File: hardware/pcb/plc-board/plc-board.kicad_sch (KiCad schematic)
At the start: 29 parts, among them J1 MAINS_L_N, J2 ESP32_UART0_PROGRAMMING, J3 ST7580_JTAG_DEBUG, U1 HLK-5M05, U2 ESP32-C3-MINI-1, U3 AMS1117-3.3, U4 ST7580, Y1 8MHz

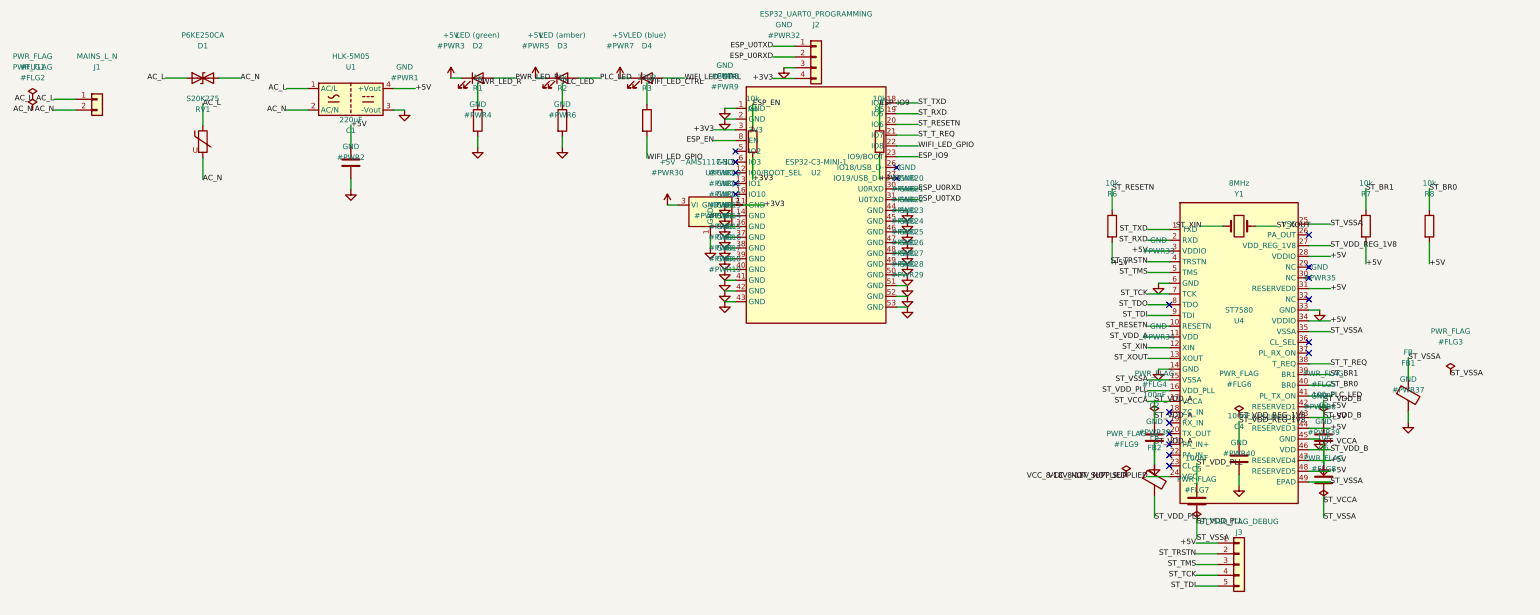
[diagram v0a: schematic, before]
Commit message: hardware: power the PLC Adapter from the Terminal, remove the inverter
Board 1's remaining gaps were meant to be a power-electronics design task:
supply the ST7580's 8-18V VCC, drive the IRF540N inverter, define its
topology. Two findings made those questions the wrong ones.

The adapter had no power source during an outage. Its only supply is the
HLK-5M05, which needs 90-264V AC. When the grid fails the adapter stops --
so it could never have run an inverter, and the 24V it was supposed to
inject could not have powered a neighbouring adapter either, despite
docs/inverter-master.md stating that a slave "listens on the wire powered
by the master's 24V injection". hardware/bom.md gives Board 1 no battery
and no supercapacitor; every battery line in that file belongs to the
Terminal. The firmware protocol had already been written against a battery
that never existed: MASTER_ALIVE carries battery_pct, MASTER_RESIGN
defines reason 0x01 = low battery.

The 24V injection was also outside EN 50065-1. The A-band limit is
134 dB(uV) at 9 kHz falling to 120 dB(uV) at 95 kHz -- 5 Vrms down to
1 Vrms -- so 24V is 5-24x over. docs/electrical-safety.md claimed the
injection was "within these limits"; it was not. The same section listed
GRIDNET among the A-band's permitted users alongside energy companies, but
the A-band is allocated to electricity suppliers and general equipment
belongs in 95-148.5 kHz. Separately, the ST7580's own PA delivers 14 V p-p
= 4.95 Vrms: ST sized the part to land on that limit, so the chip already
produces the strongest signal the standard permits.

So the adapter is now powered from the Terminal's battery over a
detachable USB-C cable, and the inverter is gone -- what it was for is
done either by that cable or by a properly-supplied power amplifier.

Board 1 schematic (29 -> 47 components, ERC clean, 0 errors):

- USB-C sink inlet (J4) with 5.1k CC strapping, power-only. It sits on the
  HLK-5M05's isolated secondary, which now matters more than before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
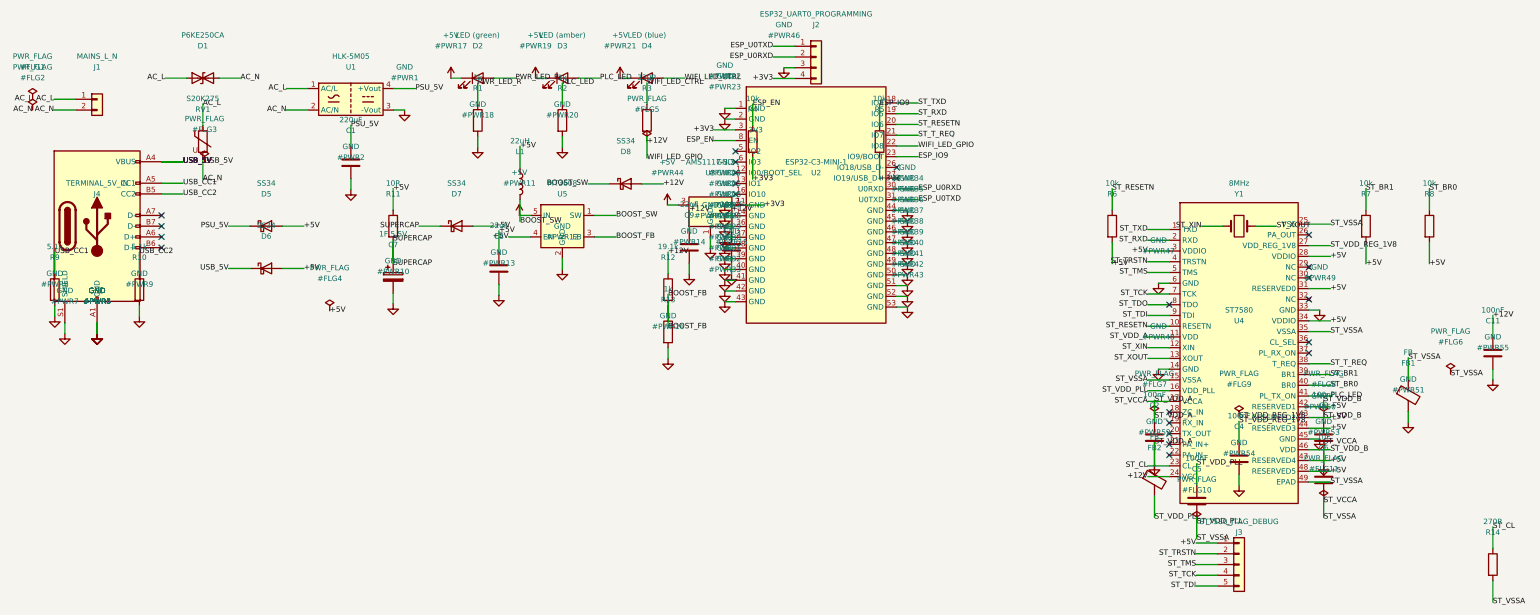
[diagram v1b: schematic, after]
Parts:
- added C10: 100uF, Capacitor_THT:CP_Radial_D6.3mm_P2.50mm, symbol Device:C
- added C11: 100nF, Capacitor_SMD:C_0603_1608Metric, symbol Device:C
- added C7: 1F 5.5V, Capacitor_THT:CP_Radial_D10.0mm_P5.00mm, symbol Device:C_Polarized
- added C8, C9: 22uF, Capacitor_SMD:C_1206_3216Metric, symbol Device:C
- added D5, D6, D7, D8: SS34, Diode_SMD:D_SMA, symbol Device:D_Schottky
- added J4: TERMINAL_5V_IN, Connector_USB:USB_C_Receptacle_HRO_TYPE-C-31-M-12, symbol Connector:USB_C_Receptacle_USB2.0_14P
- added L1: 22uH, Inductor_SMD:L_6.3x6.3_H3, symbol Device:L
- added R10, R9: 5.1k, Resistor_SMD:R_0603_1608Metric, symbol Device:R
- added R11: 10R, Resistor_SMD:R_1206_3216Metric, symbol Device:R
- added R12: 19.1k, Resistor_SMD:R_0603_1608Metric, symbol Device:R
- added R13: 1k, Resistor_SMD:R_0603_1608Metric, symbol Device:R
- added R14: 270R, Resistor_SMD:R_0603_1608Metric, symbol Device:R
- added U5: MT3608, Package_TO_SOT_SMD:SOT-23-6, symbol Regulator_Switching:MT3608
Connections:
- net WIFI_LED_GPIO is gone; now on net +12V: R3.2, U2.22 (IO8)
- net +5V: now also C8.1, D5.2 (A), D6.2 (A), D7.2 (A), L1.1, R11.1, U5.4 (EN), U5.5 (IN); no longer C1.1, U1.4 (+Vout)
- net GND: now also C10.2, C11.2, C7.2, C8.2, C9.2, J4.A1 (GND), J4.A12 (GND), J4.B1 (GND), J4.B12 (GND), J4.S1 (SHIELD), R10.2, R13.2, R14.2, R9.2, U5.2 (GND)
- net ST_CL: now reaches U4.23 (CL)
- net ST_CL: now also R14.1
- net VCC_8-18V_NOT_SUPPLIED renamed +12V
- net +12V: now also C10.1, C11.1, C9.1, D8.2 (A), R12.1
- new net BOOST_FB: R12.2, R13.1, U5.3 (FB)
- new net BOOST_SW: D8.1 (K), L1.2, U5.1 (SW)
- new net PSU_5V: C1.1, D5.1 (K), U1.4 (+Vout)
- new net SUPERCAP: C7.1, D7.1 (K), R11.2
- new net USB_5V: D6.1 (K), J4.A4 (VBUS), J4.A9 (VBUS), J4.B4 (VBUS), J4.B9 (VBUS)
- new net USB_CC1: J4.A5 (CC1), R9.1
- new net USB_CC2: J4.B5 (CC2), R10.1
- no-connect marks 20 -> 23

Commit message: hardware: build Board 1's line coupling, retuned from AN4068 to B+C
The last open block on Board 1, and the reason its PCB layout had not
started. The ST7580 datasheet specifies the PA's pins but not the network
hung off them; AN4068 does, and earlier passes could not retrieve it.

It was read through alldatasheet's HTML viewer, which carries each page's
text even though the page images come back blank. That gives the values,
the equations and the tables -- but not Figure 6 (the coupling schematic)
or Figure 14 (the zero crossing circuit), which are images with no text
layer. Where connectivity could not be read off a figure it is derived from
the equations, and docs/plc-coupling.md says so at each point.

The values are not AN4068's. Its reference design is a CENELEC A-band node:
receive filter on 80 kHz, coupling resonance on 85 kHz, receive sensitivity
specified at fC = 86 kHz. A-band is allocated to electricity suppliers
(docs/electrical-safety.md), so GRIDNET sits in B+C, 95-140 kHz -- which
puts our entire band on the skirt of their filters. Three rules, applied to
every block:

- keep AN4068's Q values, which it chose against measured mains impedance
  and a Montecarlo tolerance analysis this project cannot repeat;
- keep its ratios to the band edge rather than its absolute corners;
- move reactances, not resistors.

                        AN4068 (A-band)        this board (B+C)
  TX RC pre-filter      1.5k + 1nF, 106 kHz    1k + 1nF, 159 kHz
  TX Sallen-Key         150 kHz, Q 1.03        221 kHz, Q 1.03  (100pF -> 68pF)
  PA gain               4.3 = 12.7 dB          4.3 = 12.7 dB    (unchanged)
  RX resonance          220uH/18nF, 80 kHz     150uH/12nF, 118.6 kHz
  Line coupling         15uH/220nF, 85 kHz     12uH/150nF, 114 kHz

Every resistor keeps its reference value. That is not a stylistic choice --
it falls out of solving for the new centres with E-series parts, and it
leaves the gain and Q expressions (resistor ratios) untouched.

Each block was check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
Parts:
- added C12: 1nF C0G, Capacitor_SMD:C_0603_1608Metric, symbol Device:C
- added C13, C14: 68pF C0G, Capacitor_SMD:C_0603_1608Metric, symbol Device:C
- added C15: 12nF, Capacitor_SMD:C_0603_1608Metric, symbol Device:C
- added C16: 10uF/50V X5R, Capacitor_SMD:C_1210_3225Metric, symbol Device:C
- added C17: 150nF X1, Capacitor_THT:C_Rect_L16.5mm_W5.0mm_P15.00mm_MKT, symbol Device:C
- added L2: 150uH, Inductor_SMD:L_1210_3225Metric, symbol Device:L
- added L3: 12uH, Inductor_SMD:L_7.3x7.3_H4.5, symbol Device:L
- added R15: 1k, Resistor_SMD:R_0603_1608Metric, symbol Device:R
- added R16: 5.1k, Resistor_SMD:R_0603_1608Metric, symbol Device:R
- added R17: 22k, Resistor_SMD:R_0603_1608Metric, symbol Device:R
- added R18: 33k, Resistor_SMD:R_0603_1608Metric, symbol Device:R
- added R19: 10k, Resistor_SMD:R_0603_1608Metric, symbol Device:R
- added R20: 150R, Resistor_SMD:R_0603_1608Metric, symbol Device:R
- added T1: 750510231, gridnet_footprints:Transformer_Wuerth_750510231, symbol gridnet_parts:PLC_COUPLING_TRANSFORMER
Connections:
- net AC_L: now also C17.2
- net AC_N: now also T1.7 (SEC_B)
- net GND: now also C12.2, C14.2, C15.2, L2.2, R19.2, T1.4 (PRI_B)
- net ST_RX_IN: now reaches U4.19 (RX_IN)
- net ST_RX_IN: now also C15.1, L2.1, R20.2
- net ST_TX_OUT: now reaches U4.20 (TX_OUT)
- net ST_TX_OUT: now also R15.1
- net ST_PA_IN_P: now reaches U4.21 (PA_IN+)
- net ST_PA_IN_P: now also C14.1, R17.2
- net ST_PA_IN_N: now reaches U4.22 (PA_IN-)
- net ST_PA_IN_N: now also R18.2, R19.1
- net ST_PA_OUT: now reaches U4.26 (PA_OUT)
- net ST_PA_OUT: now also C13.2, C16.1, R18.1
- new net PLC_COUPLING: C16.2, R20.1, T1.1 (PRI_A)
- new net PLC_LINE: L3.1, T1.10 (SEC_A)
- new net PLC_LINE_X1: C17.1, L3.2
- new net ST_PA_SK: C13.1, R16.2, R17.1
- new net ST_TX_FILT: C12.1, R15.2, R16.1
- no-connect marks 23 -> 18

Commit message: hardware: place Board 1's PCB around a mains isolation barrier
plc-board.kicad_pcb places all 62 components inside the 100x80mm outline,
with thermal vias under both exposed pads and the design rules written into
plc-board.kicad_pro. Nothing is routed yet.

Structurally this is the Main Board's build_pcb.py with one thing added that
board never had to think about: half of this board is at mains potential.

  x = 0                     BARRIER_X = 30                       x = 100
  |<----- mains side ------>|<-- 7.96mm -->|<--- isolated side --->|
  | J1 mains in, TVS, MOV,  |   no copper  | ST7580 + coupling     |
  | X1 cap, series inductor |  either side | filter, ESP32, power  |
  |         U1 (HLK-5M05) --+--------------+-- tree, USB-C, LEDs   |
  |         T1 (coupling) --+--------------+                       |

Only two parts cross that band, and each crosses it inside its own body,
where the manufacturer rather than this project is responsible for the
insulation. The band's width is not a number picked here either: it is what
T1's land pattern leaves between primary and secondary once the 2.2mm pads
come off the 10.16mm pitch. Wuerth sized that gap for a transformer whose
whole job is to sit across a mains barrier.

Placement alone would not keep it that way, so three things enforce it:

- check_isolation_barrier() tests every pad of every net on the board -- not
  only the parts someone remembered to classify as mains -- against the band,
  on pad bounding boxes rather than centres, since it is the copper edge that
  matters for creepage. It also asserts that exactly U1 and T1 have pads on
  both sides. Verified by dragging C17 across the barrier and confirming the
  build refused.
- The ground pour is clipped to the isolated side. This is the one function
  that could not be reused from the Main Board unchanged: a full-width pour
  would put GND copper straight through the barrier, and would do it
  silently, because a zone is not a track and would not appe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
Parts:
- J1: footprint TerminalBlock:TerminalBlock_bornier-2_P5.08mm -> TerminalBlock:TerminalBlock_Wuerth_691311400102_P7.62mm
- U4: footprint Package_DFN_QFN:QFN-48-1EP_7x7mm_P0.5mm_EP5.1x5.1mm_ThermalVias -> Package_DFN_QFN:QFN-48-1EP_7x7mm_P0.5mm_EP5.1x5.1mm
